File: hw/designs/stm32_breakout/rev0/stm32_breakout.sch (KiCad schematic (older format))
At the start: 16 parts, among them J1 USB_B_Micro, J2 Conn_01x10_Male, J3 Conn_01x10_Male, U1 AP7361C-33ER, U2 STM32L031F6Px, U3 KC2016Z

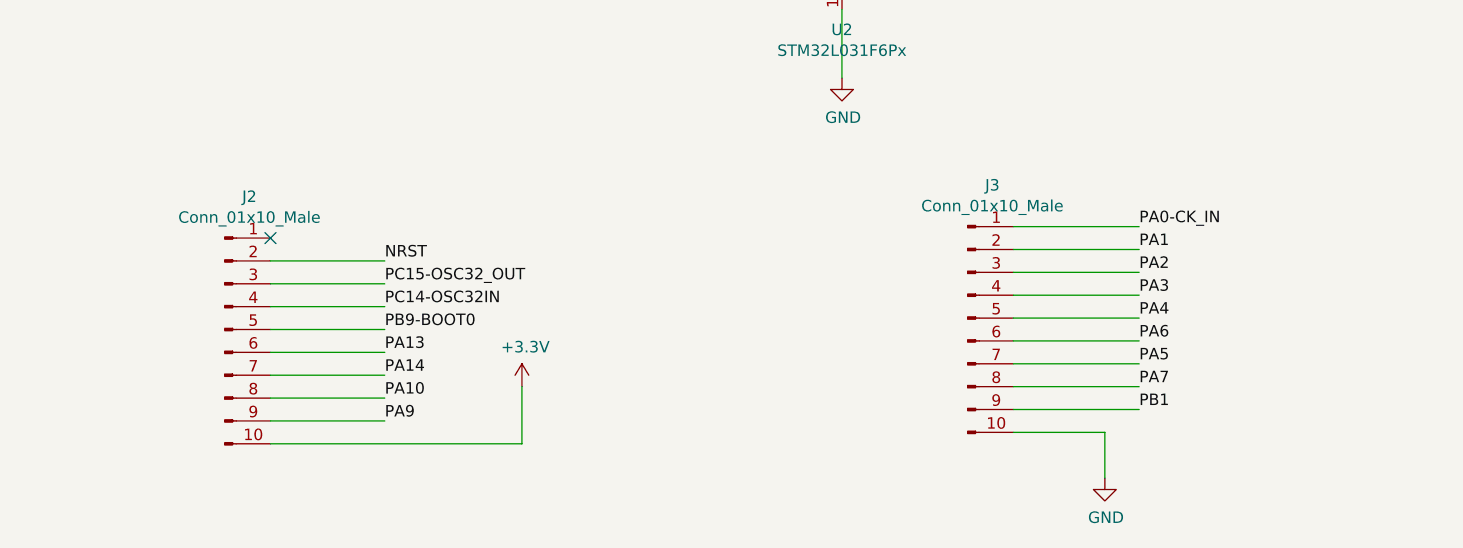
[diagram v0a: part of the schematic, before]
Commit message: Updated with SWD pins
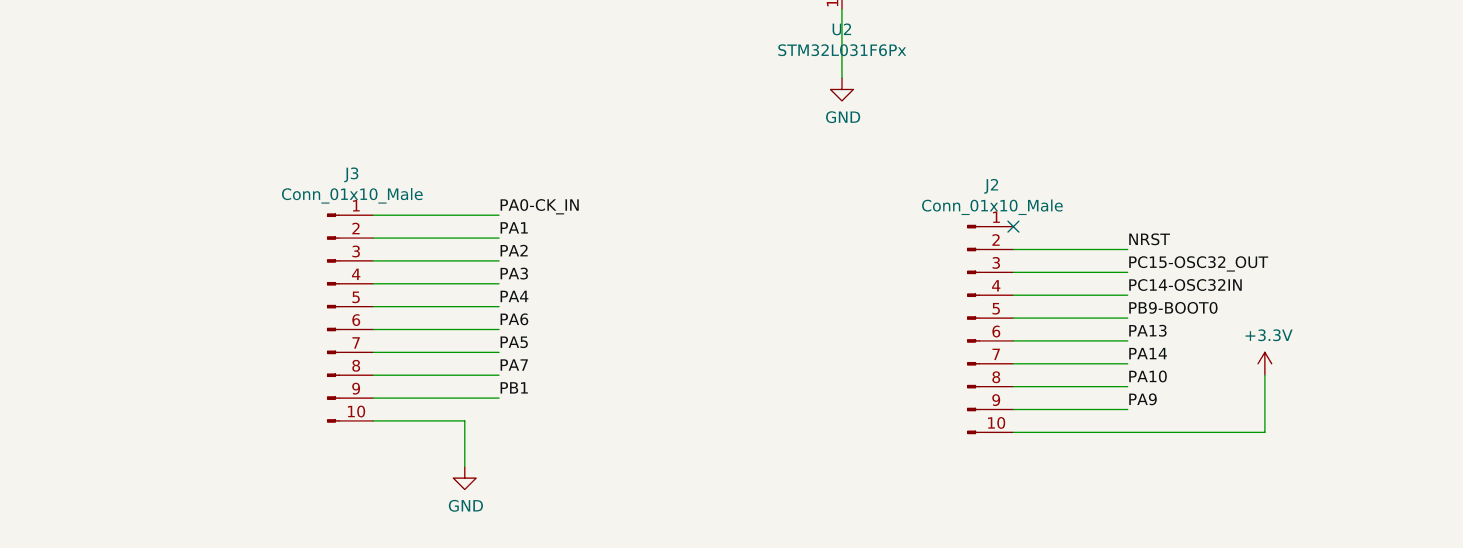
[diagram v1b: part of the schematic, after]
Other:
- moved on the sheet: J2, J3
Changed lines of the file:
@@
 L Connector:Conn_01x10_Male J3
 U 1 1 60894859
-P 6200 5400
-F 0 "J3" H 6308 5981 50  0000 C CNN
-F 1 "Conn_01x10_Male" H 6308 5890 50  0000 C CNN
-F 2 "Connector_PinSocket_2.54mm:PinSocket_1x10_P2.54mm_Vertical" H 6200 5400 50  0001 C CNN
-F 3 "~" H 6200 5400 50  0001 C CNN
-	1    6200 5400
-	1    0    0    -1
-$EndComp
-$Comp
-L Connector:Conn_01x10_Male J2
-U 1 1 60898F4F
-P 2950 5450
-F 0 "J2" H 3058 6031 50  0000 C CNN
-F 1 "Conn_01x10_Male" H 3058 5940 50  0000 C CNN
-F 2 "Connector_PinSocket_2.54mm:PinSocket_1x10_P2.54mm_Vertical" H 2950 5450 50  0001 C CNN
-F 3 "~" H 2950 5450 50  0001 C CNN
-	1    2950 5450
-	1    0    0    -1
-$EndComp
-Text Label 6950 5000 0    50   ~ 0
+P 3400 5350
+F 0 "J3" H 3508 5931 50  0000 C CNN
+F 1 "Conn_01x10_Male" H 3508 5840 50  0000 C CNN
+F 2 "Connector_PinSocket_2.54mm:PinSocket_1x10_P2.54mm_Vertical" H 3400 5350 50  0001 C CNN
+F 3 "~" H 3400 5350 50  0001 C CNN
+	1    3400 5350
+	1    0    0    -1
+$EndComp
+Text Label 4150 4950 0    50   ~ 0
 PA0-CK_IN
-Text Label 6950 5100 0    50   ~ 0
+Text Label 4150 5050 0    50   ~ 0
 PA1
-Text Label 6950 5200 0    50   ~ 0
+Text Label 4150 5150 0    50   ~ 0
 PA2
-Text Label 6950 5300 0    50   ~ 0
+Text Label 4150 5250 0    50   ~ 0
 PA3
-Text Label 6950 5700 0    50   ~ 0
+Text Label 4150 5650 0    50   ~ 0
 PA7
-Text Label 3650 5850 0    50   ~ 0
+Text Label 6900 5800 0    50   ~ 0
 PA9
-Text Label 3650 5550 0    50   ~ 0
+Text Label 6900 5500 0    50   ~ 0
 PA13
-Text Label 3650 5650 0    50   ~ 0
+Text Label 6900 5600 0    50   ~ 0
 PA14
 Wire Wire Line
-	6400 5100 6950 5100
-Wire Wire Line
-	6400 5200 6950 5200
-Wire Wire Line
-	6400 5300 6950 5300
-Wire Wire Line
-	6400 5700 6950 5700
-Text Label 3650 5350 0    50   ~ 0
+	3600 5050 4150 5050
+Wire Wire Line
+	3600 5150 4150 5150
+Wire Wire Line
+	3600 5250 4150 5250
+Wire Wire Line
+	3600 5650 4150 5650
+Text Label 6900 5300 0    50   ~ 0
 PC14-OSC32IN
-Text Label 6950 5800 0    50   ~ 0
+Text Label 4150 5750 0    50   ~ 0
 PB1
-Text Label 3650 5450 0    50   ~ 0
+Text Label 6900 5400 0    50   ~ 0
 PB9-BOOT0
-Text Label 3650 5250 0    50   ~ 0
+Text Label 6900 5200 0    50   ~ 0
 PC15-OSC32_OUT
 $Comp
@@
 L power:+3.3V #PWR06
 U 1 1 6090C2FF
-P 4250 5700
-F 0 "#PWR06" H 4250 5550 50  0001 C CNN
-F 1 "+3.3V" H 4265 5873 50  0000 C CNN
-F 2 "" H 4250 5700 50  0001 C CNN
-F 3 "" H 4250 5700 50  0001 C CNN
-	1    4250 5700
-	1    0    0    -1
-$EndComp
-Text Label 3650 5150 0    50   ~ 0
+P 7500 5650
+F 0 "#PWR06" H 7500 5500 50  0001 C CNN
+F 1 "+3.3V" H 7515 5823 50  0000 C CNN
+F 2 "" H 7500 5650 50  0001 C CNN
+F 3 "" H 7500 5650 50  0001 C CNN
+	1    7500 5650
+	1    0    0    -1
+$EndComp
+Text Label 6900 5100 0    50   ~ 0
 NRST
 $Comp
 L power:GND #PWR09
 U 1 1 6091C1DA
-P 6800 6100
-F 0 "#PWR09" H 6800 5850 50  0001 C CNN
-F 1 "GND" H 6805 5927 50  0000 C CNN
-F 2 "" H 6800 6100 50  0001 C CNN
-F 3 "" H 6800 6100 50  0001 C CNN
-	1    6800 6100
-	1    0    0    -1
-$EndComp
-Wire Wire Line
-	6800 5900 6800 6100
-Wire Wire Line
-	6400 5000 6950 5000
+P 4000 6050
+F 0 "#PWR09" H 4000 5800 50  0001 C CNN
+F 1 "GND" H 4005 5877 50  0000 C CNN
+F 2 "" H 4000 6050 50  0001 C CNN
+F 3 "" H 4000 6050 50  0001 C CNN
+	1    4000 6050
+	1    0    0    -1
+$EndComp
+Wire Wire Line
+	4000 5850 4000 6050
+Wire Wire Line
+	3600 4950 4150 4950
 $Comp
 L MCU_ST_STM32L0:STM32L031F6Px U2
@@
 NoConn ~ 2150 2800
 Wire Wire Line
-	3150 5950 4250 5950
-Wire Wire Line
-	4250 5700 4250 5950
-Wire Wire Line
-	6400 5600 6950 5600
-Wire Wire Line
-	6400 5400 6950 5400
-Text Label 6950 5600 0    50   ~ 0
+	3600 5550 4150 5550
+Wire Wire Line
+	3600 5350 4150 5350
+Text Label 4150 5550 0    50   ~ 0
 PA5
-Text Label 6950 5400 0    50   ~ 0
+Text Label 4150 5350 0    50   ~ 0
 PA4
 Wire Wire Line
-	6400 5500 6950 5500
-Text Label 6950 5500 0    50   ~ 0
+	3600 5450 4150 5450
+Text Label 4150 5450 0    50   ~ 0
 PA6
 Wire Wire Line
-	6400 5800 6950 5800
-Wire Wire Line
-	6400 5900 6800 5900
-Wire Wire Line
-	3150 5850 3650 5850
-Wire Wire Line
-	3150 5750 3650 5750
-Wire Wire Line
-	3150 5650 3650 5650
-Wire Wire Line
-	3150 5550 3650 5550
-Wire Wire Line
-	3150 5450 3650 5450
-Wire Wire Line
-	3150 5350 3650 5350
-Wire Wire Line
-	3150 5250 3650 5250
-Wire Wire Line
-	3650 5150 3150 5150
-NoConn ~ 3150 5050
-Text Label 3650 5750 0    50   ~ 0
+	3600 5750 4150 5750
+Wire Wire Line
+	3600 5850 4000 5850
+Wire Wire Line
+	6400 5800 6900 5800
+Text Label 6900 5700 0    50   ~ 0
 PA10
 Wire Wire Line
@@
 	1    0    0    -1
 $EndComp
+Wire Wire Line
+	7500 5650 7500 5900
+Wire Wire Line
+	6400 5900 7500 5900
+NoConn ~ 6400 5000
+Wire Wire Line
+	6900 5100 6400 5100
+Wire Wire Line
+	6400 5200 6900 5200
+Wire Wire Line
+	6400 5300 6900 5300
+Wire Wire Line
+	6400 5400 6900 5400
+Wire Wire Line
+	6400 5500 6900 5500
+Wire Wire Line
+	6400 5600 6900 5600
+Wire Wire Line
+	6400 5700 6900 5700
+$Comp
+L Connector:Conn_01x10_Male J2
+U 1 1 60898F4F
+P 6200 5400
+F 0 "J2" H 6308 5981 50  0000 C CNN
+F 1 "Conn_01x10_Male" H 6308 5890 50  0000 C CNN
+F 2 "Connector_PinSocket_2.54mm:PinSocket_1x10_P2.54mm_Vertical" H 6200 5400 50  0001 C CNN
+F 3 "~" H 6200 5400 50  0001 C CNN
+	1    6200 5400
+	1    0    0    -1
+$EndComp
